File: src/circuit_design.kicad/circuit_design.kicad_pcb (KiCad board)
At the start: 2 copper layers, 228.6 x 180.3 mm, 113 parts, among them J1 USB_B_Micro, U1 К176ИЕ12, U10 К155ЛА4, U11 К155ЛИ1, U12 К155ЛА1, U13 К155ИЕ5, U14 К155ЛЛ1, U15 К155ЛН1, U16 К155ЛИ1, U17 К155ТВ15, U18 К155ИЕ5, U19 К155ЛП5, U2 К155ЛП10, U20 К155ИВ1, U21 К155ИД7, U22 К155ИД4, U23 К155ЛН3, U24 К155ЛП10, U3 К155ЛЕ3, U31 К155ЛЕ1, U32 К155ЛН1, U33 К155ЛИ1, U34 К155ЛА4, U35 К155ТВ15, U4 К155ЛН1, U5 К155ЛИ1, U6 К155ЛЛ1, U9 К155ИЕ5, Y1 32768

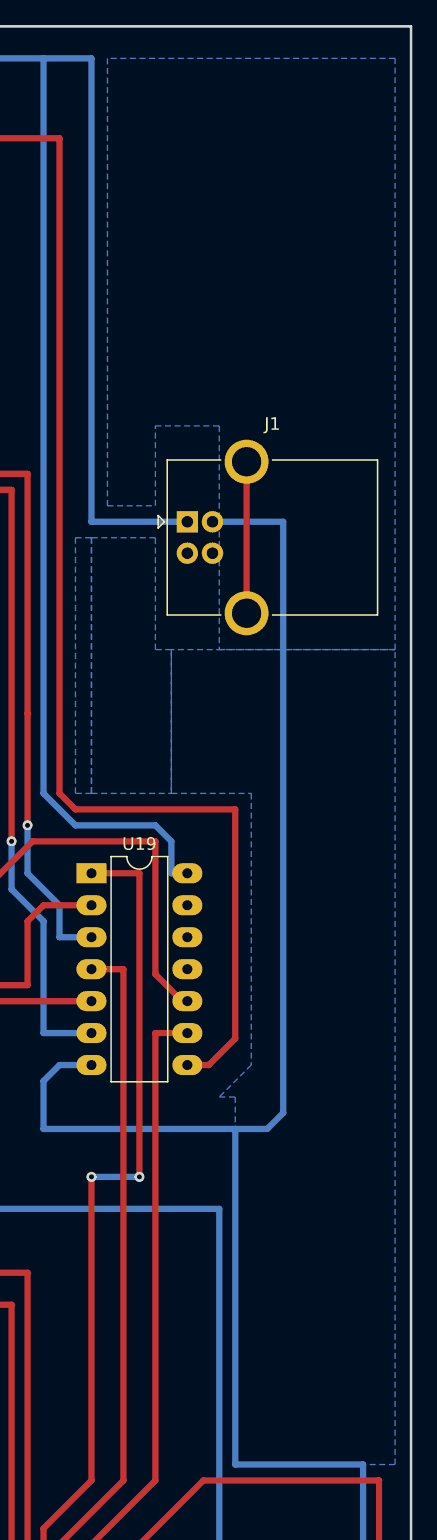
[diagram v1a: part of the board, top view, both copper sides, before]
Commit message: 01. The small refactoring was done 02. The on-power init by reset module was added
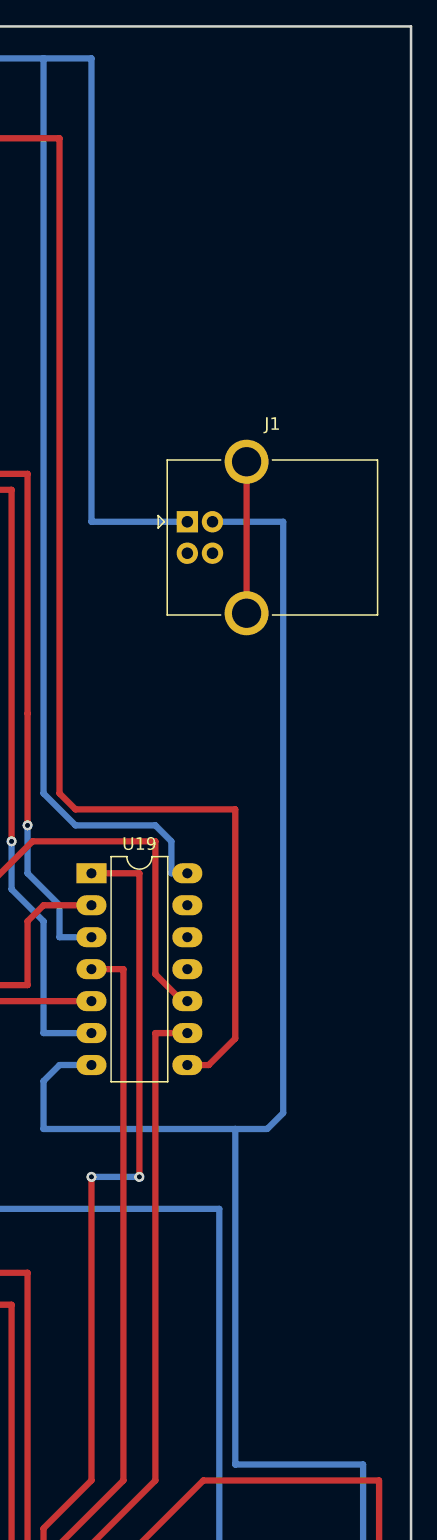
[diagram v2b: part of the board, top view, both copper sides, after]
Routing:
- removed copper zone on B.Cu, net GND
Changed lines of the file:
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@@
   (segment (start 194.31 72.39) (end 198.882 72.39) (width 0.5) (layer B.Cu) (net 38))
   (segment (start 198.882 72.39) (end 198.882 72.39) (width 0.5) (layer B.Cu) (net 38))
-  (via blind (at 198.882 72.39) (size 0.8) (drill 0.4) (layers F.Cu B.Cu) (net 38) (status 1000000))
+  (via blind (at 198.882 72.39) (size 0.8) (drill 0.4) (layers F.Cu B.Cu) (net 38))
   (segment (start 209.931 83.82) (end 207.01 83.82) (width 0.5) (layer F.Cu) (net 38))
   (segment (start 210.439 83.312) (end 209.931 83.82) (width 0.5) (layer F.Cu) (net 38))
@@
   (segment (start 207.01 101.6) (end 207.01 101.6) (width 0.5) (layer B.Cu) (net 154))
   (via blind (at 207.01 101.6) (size 0.8) (drill 0.4) (layers F.Cu B.Cu) (net 154))
-  (zone (net 2) (net_name GND) (layer B.Cu) (hatch edge 0.508)
-    (connect_pads (clearance 0.508))
-    (min_thickness 0.254)
-    (fill yes (arc_segments 32) (thermal_gap 0.508) (thermal_bridge_width 0.508))
-    (polygon
-      (pts
-        (xy 252.73 60.96) (xy 252.73 72.39) (xy 259.08 72.39) (xy 259.08 93.98) (xy 256.54 96.52)
-        (xy 257.81 96.52) (xy 257.81 125.73) (xy 270.51 125.73) (xy 270.51 60.96)
-      )
-    )
-  )
-  (zone (net 2) (net_name GND) (layer B.Cu) (hatch edge 0.508)
-    (connect_pads (clearance 0.508))
-    (min_thickness 0.254)
-    (fill yes (arc_segments 32) (thermal_gap 0.508) (thermal_bridge_width 0.508))
-    (polygon
-      (pts
-        (xy 270.51 60.96) (xy 270.51 13.97) (xy 247.65 13.97) (xy 247.65 49.53) (xy 251.46 49.53)
-        (xy 251.46 43.18) (xy 256.54 43.18) (xy 256.54 60.96)
-      )
-    )
-  )
-  (zone (net 2) (net_name GND) (layer B.Cu) (hatch edge 0.508)
-    (connect_pads (clearance 0.508))
-    (min_thickness 0.254)
-    (fill yes (arc_segments 32) (thermal_gap 0.508) (thermal_bridge_width 0.508))
-    (polygon
-      (pts
-        (xy 246.38 52.07) (xy 246.38 72.39) (xy 252.73 72.39) (xy 252.73 60.96) (xy 251.46 60.96)
-        (xy 251.46 52.07)
-      )
-    )
-  )
-  (zone (net 2) (net_name GND) (layer B.Cu) (hatch edge 0.508)
-    (connect_pads (clearance 0.508))
-    (min_thickness 0.254)
-    (fill yes (arc_segments 32) (thermal_gap 0.508) (thermal_bridge_width 0.508))
-    (polygon
-      (pts
-        (xy 246.38 72.39) (xy 245.11 72.39) (xy 245.11 52.07) (xy 246.38 52.07)
-      )
-    )
-  )
 )

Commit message: 01. Some of chips was updated to ones without common VCC to fix common powerting issue. 02. The PCB layout update was started
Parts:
- added C10: 10uF/16V, Capacitor_THT:CP_Radial_D5.0mm_P2.50mm, F.Cu at (-84.5, 133.3)
- added C11: 100nF, Capacitor_THT:C_Disc_D5.1mm_W3.2mm_P5.00mm, F.Cu at (13.3, 40.8)
- added C12: 22uF/16V, Capacitor_THT:CP_Radial_D4.0mm_P2.00mm, F.Cu at (-50.8, 143.5)
- added C13: 100uF, Capacitor_THT:CP_Radial_D5.0mm_P2.50mm, F.Cu at (28.6, 124.5)
- added C4: 474, Capacitor_THT:C_Disc_D5.1mm_W3.2mm_P5.00mm, F.Cu at (3.80, 47.3)
- added C5: 474, Capacitor_THT:C_Disc_D5.1mm_W3.2mm_P5.00mm, F.Cu at (-26.7, 13.3)
- added C6: 474, Capacitor_THT:C_Disc_D5.1mm_W3.2mm_P5.00mm, F.Cu at (-19.1, 51.4)
- added C7: 1000uF, Capacitor_THT:CP_Radial_D13.0mm_P5.00mm, F.Cu at (-98.4, 188.0)
- added C8: 100nF, Capacitor_THT:CP_Radial_D5.0mm_P2.50mm, F.Cu at (-13.3, 137.2)
- added C9: 105, Capacitor_THT:C_Disc_D5.1mm_W3.2mm_P5.00mm, F.Cu at (-89.5, 165.7)
- added CONN_BATT_REPLACE_LED_1: Conn_01x02_Male, Connector_PinHeader_2.54mm:PinHeader_1x02_P2.54mm_Vertical, F.Cu at (-108.6, 18.4)
- added CONN_SW_DPST01_TIMER_1: Conn_01x02_Male, Connector_PinHeader_2.54mm:PinHeader_2x01_P2.54mm_Vertical, F.Cu at (31.8, 84.5)
- added C_OUT_1: 105, Capacitor_THT:C_Disc_D5.1mm_W3.2mm_P5.00mm, F.Cu at (-21.6, 270.5)
- added C_OUT_2: 106, Capacitor_THT:C_Disc_D5.1mm_W3.2mm_P5.00mm, F.Cu at (-21.6, 280.0)
- added C_OUT_3: 106, Capacitor_THT:C_Disc_D5.1mm_W3.2mm_P5.00mm, F.Cu at (-21.6, 290.2)
- added C_OUT_4: 106, Capacitor_THT:C_Disc_D5.1mm_W3.2mm_P5.00mm, F.Cu at (-21.6, 300.4)
- added C_PWR_1: 1000 uF/50V, Capacitor_THT:CP_Radial_D13.0mm_P5.00mm, F.Cu at (256.5, 40.0)
- added C_PWR_2: 105, Capacitor_THT:C_Disc_D5.1mm_W3.2mm_P5.00mm, F.Cu at (268.0, 35.6)
- added C_PWR_3: 105, Capacitor_THT:C_Disc_D5.1mm_W3.2mm_P5.00mm, F.Cu at (268.0, 42.5)
- added C_PWR_4: 105, Capacitor_THT:C_Disc_D5.1mm_W3.2mm_P5.00mm, F.Cu at (264.2, 69.8)
- added C_PWR_5: 330 uF/50V, Capacitor_THT:CP_Radial_D10.0mm_P5.00mm, F.Cu at (264.2, 78.7)
- added C_PWR_6: 333, Capacitor_THT:C_Disc_D5.1mm_W3.2mm_P5.00mm, F.Cu at (261.0, 108.6)
- added D10: 1N5817, Diode_THT:D_DO-41_SOD81_P10.16mm_Horizontal, F.Cu at (-105.4, 160.0)
- added D11: 1N4007, Diode_THT:D_DO-41_SOD81_P10.16mm_Horizontal, F.Cu at (-86.4, 206.4)
- added D12: 1N4007, Diode_THT:D_DO-41_SOD81_P10.16mm_Horizontal, F.Cu at (259.7, 121.9)
- added D9: 1N4007, Diode_THT:D_DO-41_SOD81_P10.16mm_Horizontal, F.Cu at (-104.1, 167.6)
- added DB_PWR_1: RS207, Diode_THT:Diode_Bridge_19.0x3.5x10.0mm_P5.0mm, F.Cu at (267.9, 28.6)
- added D_BATT_1: SS24T3G, Package_TO_SOT_THT:TO-220-2_Vertical, F.Cu at (-101.6, 65.4)
- added D_BATT_2: SS24T3G, Package_TO_SOT_THT:TO-220-2_Vertical, F.Cu at (-101.6, 76.8)
- added D_BATT_3: SS24T3G, Package_TO_SOT_THT:TO-220-2_Vertical, F.Cu at (-100.3, 87.0)
- added D_PWR_1: MBR745, Package_TO_SOT_THT:TO-220-2_Vertical, F.Cu at (251.5, 57.8)
- added JCONN_SW_DPST02_TIMER_1: Conn_01x02_Male, Connector_PinHeader_2.54mm:PinHeader_2x01_P2.54mm_Vertical, F.Cu at (26.7, 60.3)
- added J_PWR_1: Barrel_Jack, Connector_BarrelJack:BarrelJack_Horizontal, F.Cu at (257.2, 19.1)
- added L1: 47 uH/5A, Inductor_SMD:L_7.3x7.3_H4.5, F.Cu at (254.6, 67.3)
- added Q1: BT136-600, Package_TO_SOT_THT:TO-220-3_Vertical, F.Cu at (-51.4, 236.2)
- added Q2: BT136-600, Package_TO_SOT_THT:TO-220-3_Vertical, F.Cu at (-17.1, 244.5)
- added Q3: BT136-600, Package_TO_SOT_THT:TO-220-3_Vertical, F.Cu at (20.3, 232.4)
- added Q4: BT136-600, Package_TO_SOT_THT:TO-220-3_Vertical, F.Cu at (59.7, 233.7)
- added R17: 10K, Resistor_THT:R_Axial_DIN0207_L6.3mm_D2.5mm_P15.24mm_Horizontal, F.Cu at (-62.0, 53.6)
- added R18: 100 Ohm, Resistor_THT:R_Axial_DIN0414_L11.9mm_D4.5mm_P15.24mm_Horizontal, F.Cu at (-76.2, 221.0)
- added R19: 100 Ohm, Resistor_THT:R_Axial_DIN0414_L11.9mm_D4.5mm_P15.24mm_Horizontal, F.Cu at (-41.3, 220.3)
- added R20: 100 Ohm, Resistor_THT:R_Axial_DIN0414_L11.9mm_D4.5mm_P15.24mm_Horizontal, F.Cu at (-4.45, 217.8)
- added R21: 100 Ohm, Resistor_THT:R_Axial_DIN0414_L11.9mm_D4.5mm_P15.24mm_Horizontal, F.Cu at (36.2, 219.7)
- added R22: 1KOhm, Resistor_THT:R_Axial_DIN0207_L6.3mm_D2.5mm_P15.24mm_Horizontal, F.Cu at (-67.3, 36.2)
- added R23: 1KOhm, Resistor_THT:R_Axial_DIN0207_L6.3mm_D2.5mm_P15.24mm_Horizontal, F.Cu at (-44.6, 38.3)
- added R24: 1KOhm, Resistor_THT:R_Axial_DIN0207_L6.3mm_D2.5mm_P15.24mm_Horizontal, F.Cu at (-55.9, 66.7)
- added R25: 1KOhm, Resistor_THT:R_Axial_DIN0207_L6.3mm_D2.5mm_P15.24mm_Horizontal, F.Cu at (-67.3, 18.4)
- added R26: 0.5R, Resistor_THT:R_Axial_DIN0207_L6.3mm_D2.5mm_P10.16mm_Horizontal, F.Cu at (-48.3, 114.9)
- added R27: 10K, Resistor_THT:R_Axial_DIN0207_L6.3mm_D2.5mm_P10.16mm_Horizontal, F.Cu at (-74.3, 123.2)
- added R28: 500R, Resistor_THT:R_Axial_DIN0207_L6.3mm_D2.5mm_P10.16mm_Horizontal, F.Cu at (-11.4, 10.8)
- added R29: 400R, Resistor_THT:R_Axial_DIN0207_L6.3mm_D2.5mm_P10.16mm_Horizontal, F.Cu at (-48.3, 132.1)
- added R30: 1K, Resistor_THT:R_Axial_DIN0207_L6.3mm_D2.5mm_P10.16mm_Horizontal, F.Cu at (-5.10, 21.2)
- added R_OUT_1: 39, Resistor_THT:R_Axial_DIN0207_L6.3mm_D2.5mm_P15.24mm_Horizontal, F.Cu at (-10.2, 270.5)
- added R_OUT_2: 39, Resistor_THT:R_Axial_DIN0207_L6.3mm_D2.5mm_P15.24mm_Horizontal, F.Cu at (-10.8, 280.0)
- added R_OUT_3: 39, Resistor_THT:R_Axial_DIN0207_L6.3mm_D2.5mm_P15.24mm_Horizontal, F.Cu at (-12.1, 290.2)
- added R_OUT_4: 39, Resistor_THT:R_Axial_DIN0207_L6.3mm_D2.5mm_P15.24mm_Horizontal, F.Cu at (-10.8, 300.4)
- added R_PWR_1: 15K, Resistor_THT:R_Axial_DIN0207_L6.3mm_D2.5mm_P15.24mm_Horizontal, F.Cu at (266.7, 87.0)
- added R_PWR_2: 2.4 K, Resistor_THT:R_Axial_DIN0207_L6.3mm_D2.5mm_P15.24mm_Horizontal, F.Cu at (260.4, 102.2)
- added U25: MOC3062M, Package_DIP:DIP-6_W7.62mm_LongPads, F.Cu at (-52.7, 220.3)
- added U26: MOC3062M, Package_DIP:DIP-6_W7.62mm_LongPads, F.Cu at (-20.3, 220.3)
- added U27: MOC3062M, Package_DIP:DIP-6_W7.62mm_LongPads, F.Cu at (19.1, 217.8)
- added U28: MOC3062M, Package_DIP:DIP-6_W7.62mm_LongPads, F.Cu at (57.1, 219.7)
- added U29: LM7806_TO220, Package_TO_SOT_THT:TO-220-3_Vertical, F.Cu at (-125.1, 161.9)
- added U30: SC6038, Package_SO:SO-8_5.3x6.2mm_P1.27mm, F.Cu at (-45.7, 123.8)
- added U36: К155ТЛ2, Package_DIP:DIP-14_W7.62mm_LongPads, F.Cu at (21.0, -50.8)
- added U37: 4020, Package_DIP:DIP-16_W7.62mm_LongPads, F.Cu at (48.9, -40.0)
- added U38: LM7806_TO220, Package_TO_SOT_THT:TO-220-3_Vertical, F.Cu at (261.6, 116.2)
- added U39: К155ЛН1, Package_DIP:DIP-14_W7.62mm_LongPads, F.Cu at (-15.2, -47.0)
- added U7: 4020, Package_DIP:DIP-16_W7.62mm_LongPads, F.Cu at (90.8, -40.0)
- added U8: ICL7660, Package_DIP:DIP-8_W7.62mm_LongPads, F.Cu at (-69.8, 128.9)
- added U_PWR_1: XL4015, Package_TO_SOT_SMD:TO-263-5_TabPin3, F.Cu at (264.2, 55.9)
- J1: value USB_B_Micro -> CONN_BAT; footprint Connector_USB:USB_B_OST_USB-B1HSxx_Horizontal -> Connector_PinHeader_2.54mm:PinHeader_1x03_P2.54mm_Vertical
- R1: value 500Ohm -> 200; footprint Resistor_THT:R_Axial_DIN0207_L6.3mm_D2.5mm_P15.24mm_Horizontal -> Resistor_THT:R_Axial_DIN0207_L6.3mm_D2.5mm_P10.16mm_Horizontal
- U23: value К155ЛН3 -> К155ЛН1
- moved J1 323.9 mm to (-64.1, -10.2)
- moved G*** 61.7 mm to (130.7, 240.5)
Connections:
- net Net-(U1-Pad10) renamed CLK_MIN
- C1 pad 1: /Control(Ext.) -> Net-(C1-Pad1)
- CONN_PWR_LINE1_13 pad 2: GND -> GNDREF
- CONN_PWR_LINE2_14 pad 2: GND -> GNDREF
- CONN_PWR_LINE3_15 pad 2: GND -> GNDREF
- CONN_PWR_LINE4_16 pad 2: GND -> GNDREF
- CONN_SW_PUSH_CONTROL_1 pad 1: +5V -> GND
- CONN_SW_PUSH_CONTROL_1 pad 2: Net-(CONN_SW_PUSH_CONTROL_1-Pad2) -> Net-(C1-Pad1)
- J1 pad 1: +5V -> BATT_OUT_+
- J1 pad 2: Net-(J1-Pad2) -> BATT_OUT_MID
- J1 pad 3: Net-(J1-Pad3) -> GND
- R1 pad 1: Net-(CONN_SW_PUSH_CONTROL_1-Pad2) -> GND
- R1 pad 2: /Control(Ext.) -> Net-(CONN_BATT_REPLACE_LED_1-Pad2)
- R4 pad 1: /Control(Ext.) -> +5V
- R4 pad 2: GND -> Net-(C1-Pad1)
- U1 pad 16: +5V -> PWR_ALW
- U1 pad 6: Net-(U1-Pad6) -> CLK_SEC
- U11 pad 1: Net-(U1-Pad4) -> Net-(U1-Pad11)
- U12 pad 10: (no net) -> Net-(U12-Pad10)
- U12 pad 12: (no net) -> Net-(U12-Pad12)
- U12 pad 13: (no net) -> Net-(U12-Pad13)
- U12 pad 14: +5V -> PWR_ALW
- U12 pad 3: Net-(U12-Pad3) -> (no net)
- U12 pad 8: (no net) -> Net-(JCONN_SW_DPST02_TIMER_1-Pad1)
- U12 pad 9: (no net) -> Net-(U12-Pad9)
- U14 pad 10: (no net) -> Net-(U14-Pad10)
- U14 pad 8: (no net) -> /Reset(Out)
- U14 pad 9: (no net) -> Net-(CONN_SW_DPST01_TIMER_1-Pad2)
- U15 pad 3: /Comparison.Equal -> Net-(U15-Pad3)
- U17 pad 1: Net-(U17-Pad1) -> Net-(U15-Pad4)
- U17 pad 10: (no net) -> Net-(U17-Pad10)
- U17 pad 11: (no net) -> Net-(U17-Pad11)
- U17 pad 12: (no net) -> Net-(U17-Pad12)
- U17 pad 13: (no net) -> Net-(U17-Pad13)
- U17 pad 14: (no net) -> Net-(U17-Pad14)
- U17 pad 15: (no net) -> Net-(U17-Pad15)
- U17 pad 16: +5V -> PWR_ALW
- U17 pad 3: Net-(U15-Pad4) -> /Comparison.Equal
- U17 pad 9: (no net) -> Net-(U17-Pad9)
- U18 pad 2: /Reset(Out) -> Net-(U18-Pad2)
- U18 pad 3: /Reset(Out) -> Net-(U18-Pad2)
- U19 pad 11: (no net) -> Net-(U14-Pad10)
- U19 pad 12: (no net) -> Net-(R30-Pad1)
- U19 pad 13: (no net) -> Net-(C13-Pad1)
- U23 pad 2: Net-(CONN_PWR_LINE1_13-Pad1) -> Net-(R18-Pad1)
- U23 pad 4: Net-(CONN_PWR_LINE2_14-Pad1) -> Net-(R19-Pad1)
- U23 pad 6: Net-(CONN_PWR_LINE3_15-Pad1) -> Net-(R20-Pad1)
- U23 pad 8: Net-(CONN_PWR_LINE4_16-Pad1) -> Net-(R21-Pad1)
- U31 pad 11: Net-(U31-Pad11) -> /Reset(Out)
- U31 pad 12: Net-(U31-Pad12) -> /Completed(In)
- U31 pad 9: Net-(U31-Pad11) -> Net-(CONN_SW_DPST01_TIMER_1-Pad2)
- U32 pad 5: Net-(U32-Pad5) -> Net-(CONN_SW_DPST01_TIMER_1-Pad1)
- U32 pad 6: Net-(U31-Pad12) -> Net-(U32-Pad6)
- U32 pad 8: /Reset(Out) -> Net-(U18-Pad2)
- U33 pad 11: (no net) -> Net-(CONN_BATT_REPLACE_LED_1-Pad1)
- U33 pad 12: (no net) -> CLK_SEC
- U33 pad 13: (no net) -> Net-(U17-Pad9)
- U33 pad 4: Net-(U32-Pad2) -> Net-(U33-Pad4)
- U33 pad 6: Net-(U31-Pad11) -> Net-(CONN_SW_DPST01_TIMER_1-Pad2)
- U34 pad 1: Net-(U32-Pad2) -> Net-(U34-Pad1)
- U34 pad 10: (no net) -> Net-(U32-Pad6)
- U34 pad 11: (no net) -> Net-(JCONN_SW_DPST02_TIMER_1-Pad1)
- U34 pad 12: Net-(U32-Pad5) -> Net-(U17-Pad15)
- U34 pad 13: /Running(Out) -> Net-(U34-Pad13)
- U34 pad 14: +5V -> PWR_ALW
- U34 pad 2: Net-(U32-Pad4) -> Net-(U34-Pad2)
- U34 pad 3: (no net) -> Net-(JCONN_SW_DPST02_TIMER_1-Pad2)
- U34 pad 4: (no net) -> Net-(U31-Pad1)
- U34 pad 5: (no net) -> PWR_ALW
- U34 pad 6: (no net) -> Net-(U33-Pad4)
- U34 pad 8: (no net) -> Net-(U34-Pad8)
- U34 pad 9: (no net) -> PWR_ALW
- U35 pad 1: Net-(U31-Pad4) -> +5V
- U35 pad 13: +5V -> GND
- U35 pad 15: Net-(U17-Pad1) -> Net-(U15-Pad4)
- U35 pad 3: +5V -> GND
- U35 pad 5: +5V -> Net-(U31-Pad4)
- U35 pad 6: /Running(Out) -> Net-(U33-Pad5)
- U35 pad 7: Net-(U33-Pad5) -> /Running(Out)
- U6 pad 13: Net-(U17-Pad1) -> Net-(U15-Pad3)
- U6 pad 6: Net-(U17-Pad1) -> Net-(U15-Pad3)
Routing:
- net BATT_OUT_-: track 0.00 -> 112.2 mm, vias 0 -> 1
- net Net-(C_PWR_6-Pad2): track 0.00 -> 77.6 mm
- net +9V: track 0.00 -> 57.4 mm
- net Net-(C_PWR_1-Pad1): track 0.00 -> 44.3 mm
- net Net-(D_PWR_1-Pad1): track 0.00 -> 32.0 mm
- net GND: track 1736.4 -> 1714.3 mm
- net +5V: track 1874.7 -> 1896.4 mm, vias 1 -> 2
- net Net-(J1-Pad5): track 12.0 -> 0.00 mm
- net VAC: track 0.00 -> 9.82 mm
- net GNDREF: track 0.00 -> 9.64 mm
- net Net-(C_PWR_3-Pad2): track 0.00 -> 7.77 mm
- net Net-(D11-Pad2): track 0.00 -> 7.03 mm
- net /Control(Ext.): track 227.7 -> 221.3 mm

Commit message: The PCB layout was updated:   - AC circuit was located
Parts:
- R22, R23, R24, R25: footprint Resistor_THT:R_Axial_DIN0207_L6.3mm_D2.5mm_P15.24mm_Horizontal -> Resistor_THT:R_Axial_DIN0207_L6.3mm_D2.5mm_P10.16mm_Horizontal
- moved R25 292.8 mm to (169.5, 190.5)
- moved C_OUT_4 235.6 mm to (184.8, 186.7), turned to 270 degrees
- moved R24 234.2 mm to (142.9, 190.5)
- moved R22 228.3 mm to (100.3, 191.1)
- moved R23 224.6 mm to (120.0, 191.1)
- moved R_OUT_4 221.9 mm to (184.8, 195.6), turned to 180 degrees
- moved R18 218.1 mm to (123.8, 134.0)
- moved C_OUT_3 210.7 mm to (161.9, 186.7), turned to 270 degrees
- moved R_OUT_3 198.1 mm to (161.9, 195.6), turned to 180 degrees
- moved R19 188.7 mm to (123.8, 128.9)
- moved C_OUT_2 185.8 mm to (139.1, 186.7), turned to 270 degrees
- moved Q1 173.3 mm to (113.7, 183.5)
- moved R_OUT_2 172.0 mm to (139.1, 195.6), turned to 180 degrees
- moved Q2 165.3 mm to (136.5, 183.5)
- moved C_OUT_1 161.3 mm to (116.2, 186.7), turned to 270 degrees
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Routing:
- net VAC: track 9.82 -> 413.3 mm, vias 0 -> 4
- net GNDREF: track 9.64 -> 368.0 mm
- net GND: track 1714.3 -> 1904.5 mm, vias 3 -> 4
- net BATT_OUT_-: track 112.2 -> 0.00 mm, vias 1 -> 0
- net Net-(R21-Pad2): track 0.00 -> 109.5 mm, vias 0 -> 2
- net Net-(R18-Pad2): track 0.00 -> 99.8 mm, vias 0 -> 4
- net Net-(R19-Pad2): track 0.00 -> 71.5 mm, vias 0 -> 5
- net Net-(R20-Pad2): track 0.00 -> 65.0 mm, vias 0 -> 5
- net Net-(R19-Pad1): track 0.00 -> 43.4 mm
- net Net-(R20-Pad1): track 0.00 -> 33.4 mm
- net Net-(R18-Pad1): track 0.00 -> 27.2 mm
- net Net-(R24-Pad1): track 0.00 -> 18.5 mm
- net Net-(R23-Pad1): track 0.00 -> 17.6 mm
- net Net-(R21-Pad1): track 0.00 -> 16.2 mm
- net Net-(R22-Pad1): track 0.00 -> 14.4 mm
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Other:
- board size 228.6 x 180.3 mm -> 231.8 x 188.6 mm

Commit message: The PCB layout was updated:   - The battery module was updated
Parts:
- R17: footprint Resistor_THT:R_Axial_DIN0207_L6.3mm_D2.5mm_P15.24mm_Horizontal -> Resistor_THT:R_Axial_DIN0207_L6.3mm_D2.5mm_P10.16mm_Horizontal
- moved R30 270.7 mm to (257.2, 88.3), turned to 90 degrees
- moved CONN_BATT_REPLACE_LED_1 243.8 mm to (130.2, 67.9)
- moved C13 236.1 mm to (258.4, 70.5)
- moved U36 190.6 mm to (101.6, 121.9), turned to 270 degrees
- moved U7 175.1 mm to (-68.6, 32.4), turned to 270 degrees
- moved C5 158.8 mm to (64.2, 143.5)
- moved C6 141.5 mm to (89.5, 142.2)
- moved D11 125.3 mm to (-71.9, 81.9)
- moved U39 118.9 mm to (-86.4, 48.3)
- moved C7 114.4 mm to (-47.0, 85.7)
- moved C8 103.9 mm to (-69.2, 49.5), turned to 180 degrees
- moved C4 103.1 mm to (56.5, 135.9), turned to 90 degrees
- moved U29 93.2 mm to (-85.7, 77.5), turned to 90 degrees
- moved J1 92.6 mm to (-32.4, 76.8)
- moved R27 86.4 mm to (-51.4, 39.8), turned to 270 degrees
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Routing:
- net GND: track 1904.5 -> 2093.8 mm, vias 4 -> 5
- net BATT_OUT_+: track 0.00 -> 106.4 mm, vias 0 -> 2
- net BATT_OUT_MID: track 0.00 -> 65.2 mm
- net Net-(C1-Pad1): track 0.00 -> 55.5 mm, vias 0 -> 3
- net /Control(Ext.): track 221.3 -> 268.6 mm
- net Net-(D10-Pad2): track 0.00 -> 45.4 mm
- net PWR_ALW: track 0.00 -> 42.2 mm
- net +9V: track 57.4 -> 97.8 mm
- net Net-(U32-Pad5): track 39.9 -> 0.00 mm
- net Net-(CONN_SW_DPST01_TIMER_1-Pad1): track 0.00 -> 39.9 mm
- net Net-(R28-Pad2): track 0.00 -> 34.7 mm
- net Net-(C13-Pad1): track 0.00 -> 13.5 mm
- net Net-(R26-Pad2): track 0.00 -> 12.4 mm
- net /Control(Ext.2): track 32.7 -> 44.8 mm
- net Net-(R27-Pad2): track 0.00 -> 12.0 mm
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
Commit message: The PCB layout was updated
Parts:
- R2, R3, R4, R7, R_OUT_1, R_OUT_2, R_OUT_3, R_OUT_4: footprint Resistor_THT:R_Axial_DIN0207_L6.3mm_D2.5mm_P15.24mm_Horizontal -> Resistor_THT:R_Axial_DIN0207_L6.3mm_D2.5mm_P10.16mm_Horizontal
- moved U37 192.5 mm to (170.8, 106.0), turned to 90 degrees
- moved J1 187.2 mm to (144.8, 16.5)
- moved C12 184.3 mm to (138.4, 17.1)
- moved C11 183.2 mm to (131.4, 17.1)
- moved C9 182.9 mm to (120.7, 23.5)
- moved D_BATT_1 170.5 mm to (125.1, 16.5)
- moved C7 167.1 mm to (107.3, 21.6)
- moved U7 159.0 mm to (89.5, 15.9)
- moved C8 158.9 mm to (88.3, 28.6)
- moved R17 153.9 mm to (93.3, 24.6)
- moved R26 153.9 mm to (97.2, 14.4)
- moved R27 153.9 mm to (100.3, 14.4)
- moved U39 150.5 mm to (60.3, 14.6)
- moved R28 148.6 mm to (82.0, 35.4)
- moved R29 148.6 mm to (71.8, 31.8)
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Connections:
- U1 pad 1: Net-(U1-Pad1) -> (no net)
- U1 pad 14: Net-(U1-Pad14) -> (no net)
- U1 pad 15: Net-(U1-Pad15) -> (no net)
- U1 pad 2: Net-(U1-Pad2) -> (no net)
- U1 pad 3: Net-(U1-Pad3) -> (no net)
- U13 pad 12: Net-(U13-Pad12) -> (no net)
- U13 pad 13: Net-(U13-Pad13) -> (no net)
- U13 pad 14: Net-(U13-Pad14) -> (no net)
- U13 pad 4: Net-(U13-Pad4) -> (no net)
- U13 pad 6: Net-(U13-Pad6) -> (no net)
- U13 pad 7: Net-(U13-Pad7) -> (no net)
- U17 pad 10: Net-(U17-Pad10) -> (no net)
- U17 pad 12: Net-(U17-Pad12) -> (no net)
- U17 pad 13: Net-(U17-Pad13) -> (no net)
- U17 pad 14: Net-(U17-Pad14) -> (no net)
- U17 pad 7: Net-(U17-Pad7) -> (no net)
- U18 pad 12: Net-(U18-Pad12) -> (no net)
- U18 pad 13: Net-(U18-Pad13) -> (no net)
- U18 pad 14: Net-(U18-Pad14) -> (no net)
- U18 pad 4: Net-(U18-Pad4) -> (no net)
- U18 pad 6: Net-(U18-Pad6) -> (no net)
- U18 pad 7: Net-(U18-Pad7) -> (no net)
- U20 pad 14: Net-(U20-Pad14) -> (no net)
- U20 pad 15: Net-(U20-Pad15) -> (no net)
- U22 pad 10: Net-(U22-Pad10) -> (no net)
- U22 pad 11: Net-(U22-Pad11) -> (no net)
- U22 pad 12: Net-(U22-Pad12) -> (no net)
- U22 pad 14: Net-(U22-Pad14) -> (no net)
- U22 pad 15: Net-(U22-Pad15) -> (no net)
- U22 pad 9: Net-(U22-Pad9) -> (no net)
- U24 pad 11: Net-(U24-Pad11) -> (no net)
- U24 pad 12: Net-(U24-Pad12) -> (no net)
- U24 pad 13: Net-(U24-Pad13) -> (no net)
- U24 pad 14: Net-(U24-Pad14) -> (no net)
- U25 pad 3: Net-(U25-Pad3) -> (no net)
- U25 pad 5: Net-(U25-Pad5) -> (no net)
- U26 pad 3: Net-(U26-Pad3) -> (no net)
- U26 pad 5: Net-(U26-Pad5) -> (no net)
- U27 pad 3: Net-(U27-Pad3) -> (no net)
- U27 pad 5: Net-(U27-Pad5) -> (no net)
- U28 pad 3: Net-(U28-Pad3) -> (no net)
- U28 pad 5: Net-(U28-Pad5) -> (no net)
- U37 pad 1: Net-(U37-Pad1) -> (no net)
- U37 pad 14: Net-(U37-Pad14) -> (no net)
- U37 pad 2: Net-(U37-Pad2) -> (no net)
- U37 pad 3: Net-(U37-Pad3) -> (no net)
- U37 pad 5: Net-(U37-Pad5) -> (no net)
- U37 pad 6: Net-(U37-Pad6) -> (no net)
- U37 pad 7: Net-(U37-Pad7) -> (no net)
- U37 pad 9: Net-(U37-Pad9) -> (no net)
- U7 pad 1: Net-(U7-Pad1) -> (no net)
- U7 pad 15: Net-(U7-Pad15) -> (no net)
- U7 pad 2: Net-(U7-Pad2) -> (no net)
- U7 pad 3: Net-(U7-Pad3) -> (no net)
- U7 pad 4: Net-(U7-Pad4) -> (no net)
- U7 pad 5: Net-(U7-Pad5) -> (no net)
- U7 pad 6: Net-(U7-Pad6) -> (no net)
- U7 pad 7: Net-(U7-Pad7) -> (no net)
- U7 pad 9: Net-(U7-Pad9) -> (no net)
- U8 pad 1: Net-(U8-Pad1) -> (no net)
- U8 pad 6: Net-(U8-Pad6) -> (no net)
- U8 pad 7: Net-(U8-Pad7) -> (no net)
- U9 pad 13: Net-(U9-Pad13) -> (no net)
- U9 pad 4: Net-(U9-Pad4) -> (no net)
- U9 pad 6: Net-(U9-Pad6) -> (no net)
- U9 pad 7: Net-(U9-Pad7) -> (no net)
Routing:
- net PWR_ALW: track 42.2 -> 567.2 mm, vias 0 -> 14
- net Net-(D11-Pad2): track 7.03 -> 412.5 mm, vias 0 -> 2
- net +9V: track 97.8 -> 347.4 mm, vias 0 -> 2
- net CLK_SEC: track 0.00 -> 223.1 mm, vias 0 -> 6
- net /Control(Ext.): track 268.6 -> 61.2 mm, vias 2 -> 1
- net Net-(CONN_SW_DPST01_TIMER_1-Pad2): track 0.00 -> 205.9 mm, vias 0 -> 8
- net CLK_MIN: track 188.0 -> 379.4 mm, vias 0 -> 7
- net Net-(U1-Pad11): track 0.00 -> 182.8 mm, vias 0 -> 7
- net Net-(U17-Pad15): track 0.00 -> 182.0 mm, vias 0 -> 10
- net Net-(U17-Pad11): track 0.00 -> 175.6 mm, vias 0 -> 3
- net Net-(JCONN_SW_DPST02_TIMER_1-Pad1): track 0.00 -> 174.3 mm, vias 0 -> 5
- net Net-(U1-Pad4): track 170.4 -> 12.8 mm
- net Net-(U18-Pad2): track 0.00 -> 150.4 mm, vias 0 -> 7
- net Net-(U34-Pad8): track 0.00 -> 147.6 mm, vias 0 -> 8
- net Net-(U17-Pad1): track 220.4 -> 80.0 mm, vias 6 -> 2
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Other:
- board size 231.8 x 188.6 mm -> 220.3 x 182.9 mm
- board text added: "Idea: Anatoly Baranovsky"
- board text added: "Made in Universe @ 2019 by Rostyslav Nikitin"
- board text removed: "Made in Universe @ 2019"
- board text removed: "by Rostyslav Nikitin & Anatoly Baranovsky"
